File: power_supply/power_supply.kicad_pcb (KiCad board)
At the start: 2 copper layers, 74 x 39 mm, 20 parts, among them J2 Conn_01x10_Pin, J3 Conn_01x10_Pin, Q1 IRF644PBF, U1 MAX1771ESA+T

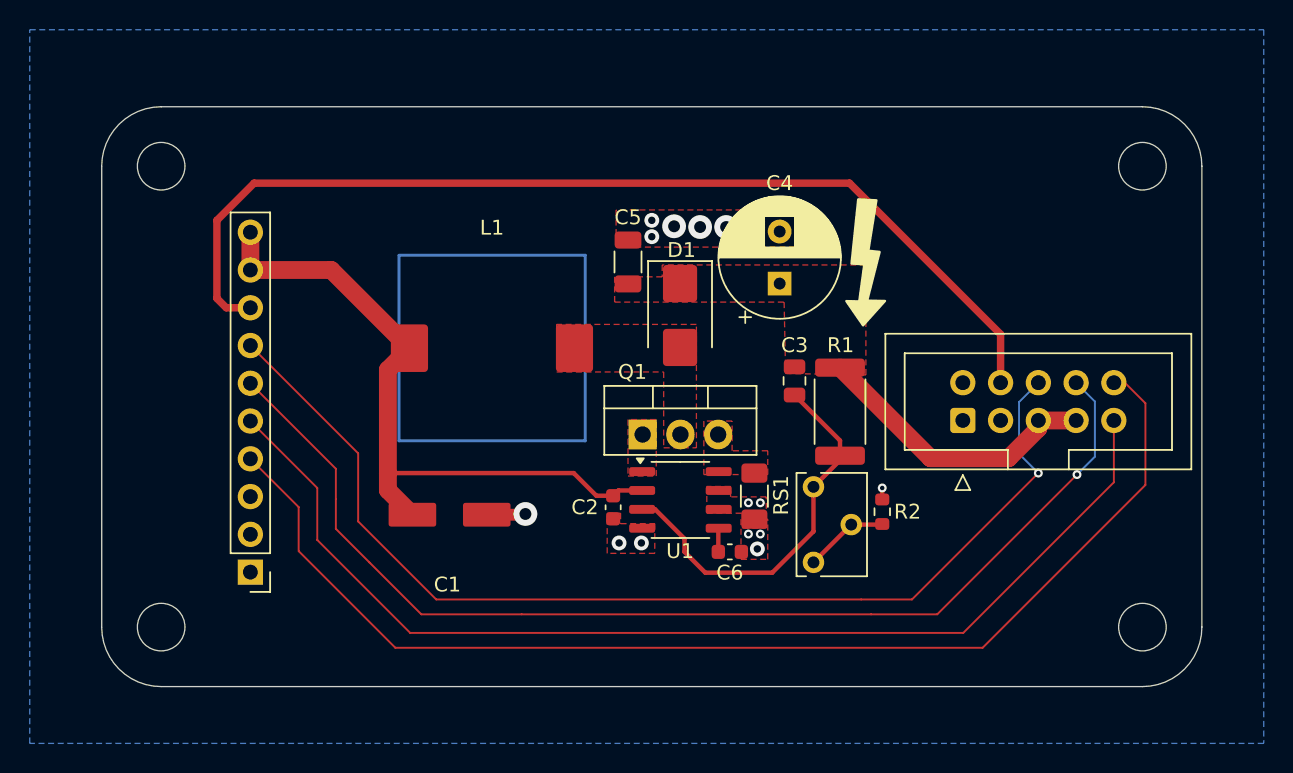
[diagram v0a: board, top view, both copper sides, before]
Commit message: Changed connectors
Changed connector from mcu to power supply to idc.
All switches now use a straight pinheader, with no pullups (now using
mcu pulldowns).
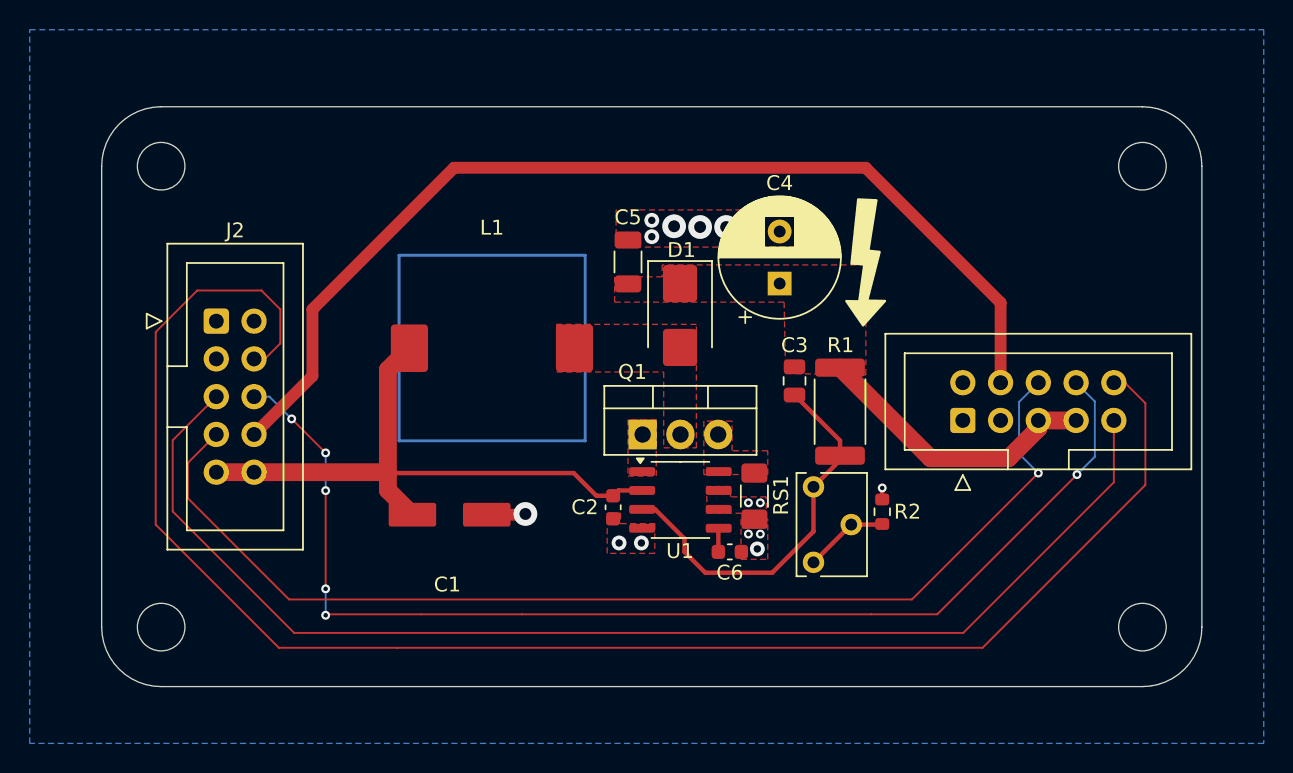
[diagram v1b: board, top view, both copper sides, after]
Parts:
- J2: footprint Connector_PinHeader_2.54mm:PinHeader_1x10_P2.54mm_Vertical -> Connector_IDC:IDC-Header_2x05_P2.54mm_Vertical
- moved J2 17.0 mm to (123.7, 80.4), turned to 0 degrees
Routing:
- net LATCH: track 79.9 -> 110.2 mm
- net CLK: track 74.4 -> 84.0 mm
- net VBUS: track 45.8 -> 41.9 mm
- net OE: track 75.5 -> 79.0 mm, vias 1 -> 6
- net SER: track 73.4 -> 75.8 mm

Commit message: Changed main PCB mount
Changed nixie board pcb mount, so now screws are visible on the front
side of the board instead of the back. Also changed mcu i2c pullups to
2k2.
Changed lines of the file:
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@@
 	(title_block
 		(title "Power Supply PCB")
-		(date "2024-06-06")
-		(rev "0.1.1")
+		(date "2024-06-16")
+		(rev "0.1.2")
 	)
 	(layers
@@
 			(at 1.27 -6.1 0)
 			(layer "F.SilkS")
-			(effects
-				(font
+			(hide yes)
+			(effects
+				(font
